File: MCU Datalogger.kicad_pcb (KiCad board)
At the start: 2 copper layers, 52.1 x 33 mm, 31 parts, among them J1 Conn_01x04_Pin, J2 Conn_01x09_Pin, J3 Conn_01x04_Pin, J4 Conn_02x03_Odd_Even, U1 DS1337S+, U2 24LC1025, U3 24LC1025, U4 ATMEGA328P-AU, Y1 32.768 KHz, Y2 16 MHz

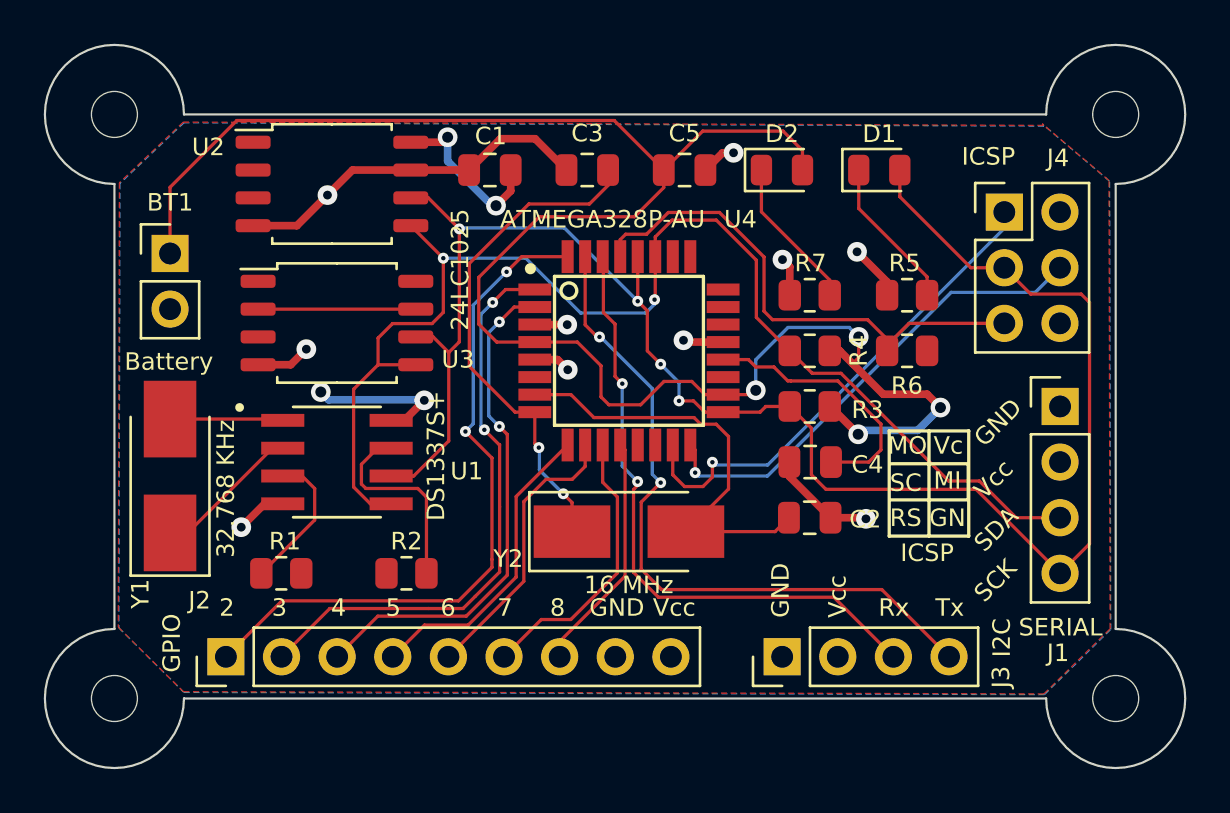
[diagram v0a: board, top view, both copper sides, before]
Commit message: Fixed issue with I2C SCL.
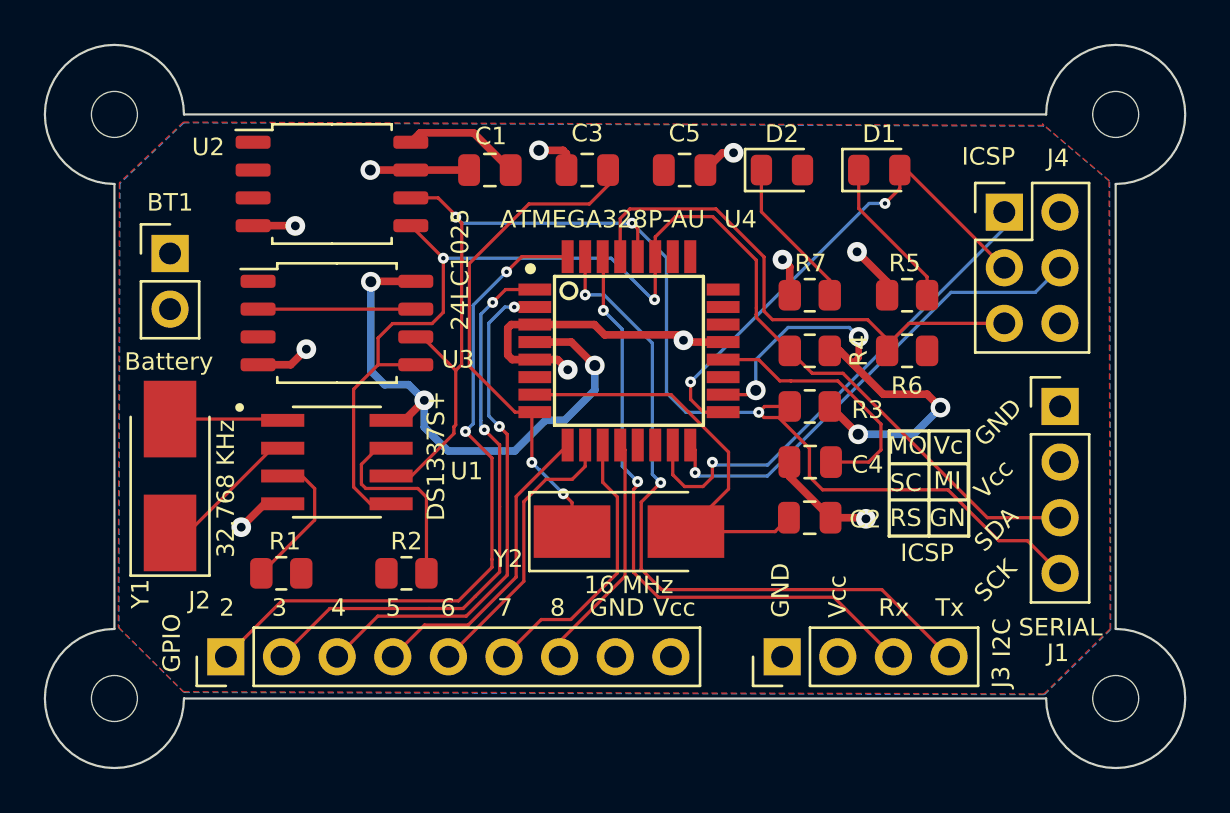
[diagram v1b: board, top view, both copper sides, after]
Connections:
- net Net-(U4-AREF) renamed /Abc123
- J1 pad 4: /SCK -> /SCL
- R3 pad 2: /SCK -> /SCL
- U1 pad 6: /SCK -> /SCL
- U2 pad 6: /SCK -> /SCL
- U3 pad 6: /SCK -> /SCL
- U4 pad 28: /SCK -> /SCL
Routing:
- net /SCL: track 0.00 -> 60.6 mm, vias 0 -> 3
- net /SCK: track 82.3 -> 23.2 mm, vias 4 -> 2
- net /Vcc: track 100.0 -> 53.4 mm, vias 8 -> 7
- net GND: track 37.7 -> 39.1 mm, vias 10 -> 11
- net /RESET: track 23.9 -> 24.6 mm
